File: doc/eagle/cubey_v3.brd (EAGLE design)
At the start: 65 x 56 mm, 24 parts, among them K1 PIN20X2

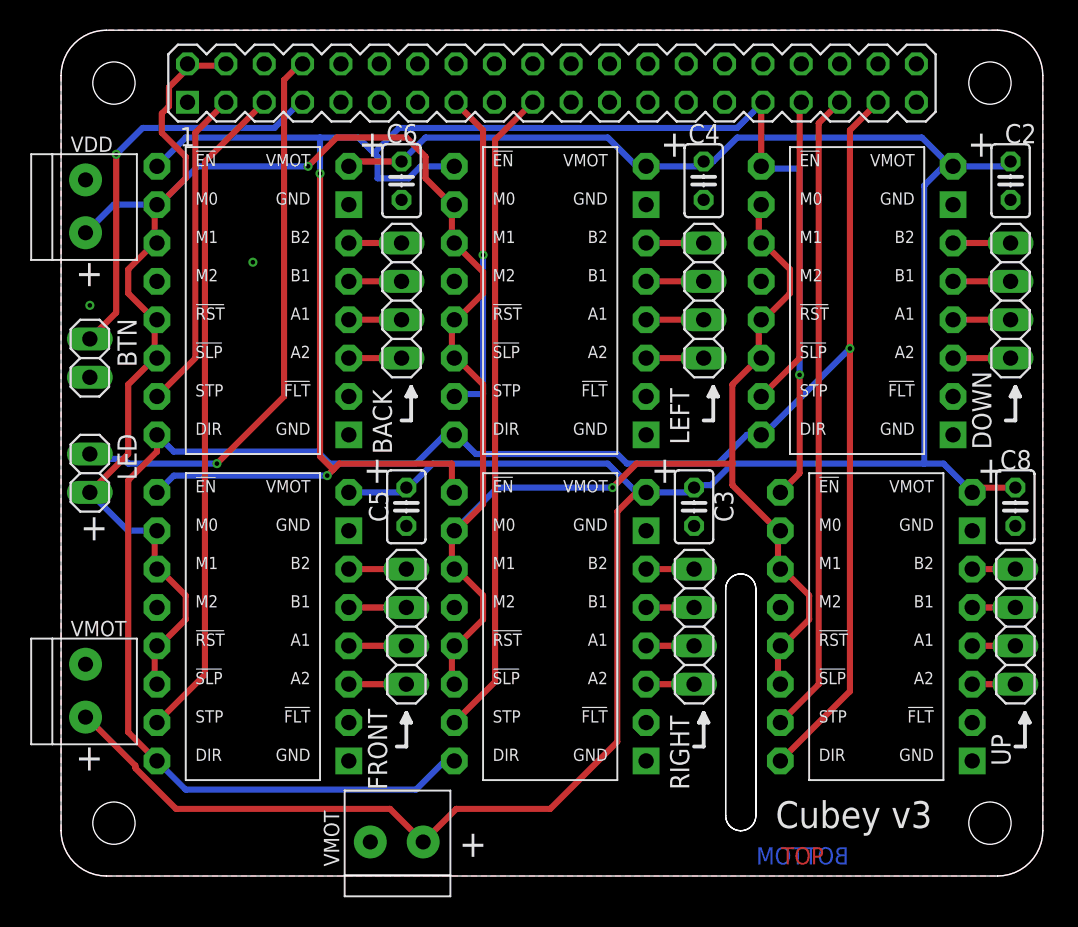
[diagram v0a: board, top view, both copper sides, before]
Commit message: Update v3 board layout, with cutout for RPi camera, remove of v2 designs
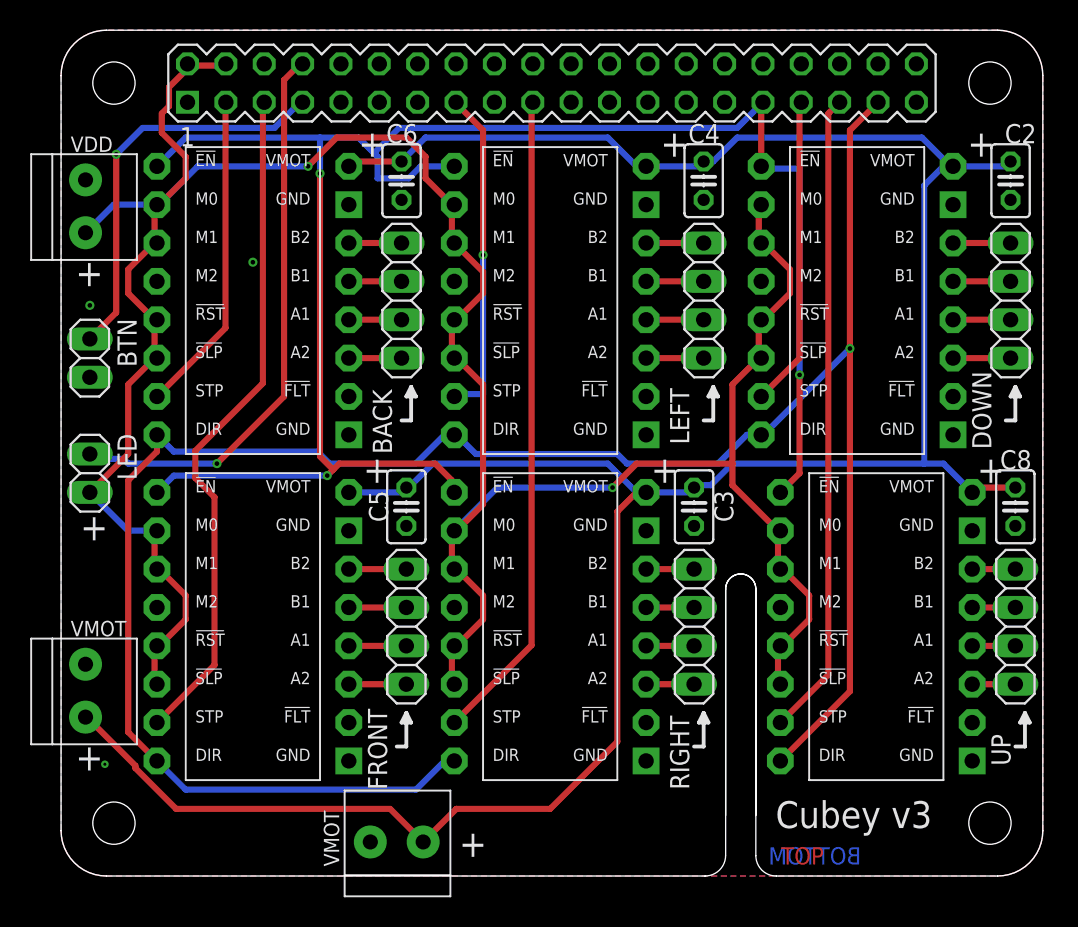
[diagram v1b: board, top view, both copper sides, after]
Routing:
- net FRONT: track 44.0 -> 45.1 mm
- net !EN_MOT: track 123.4 -> 122.7 mm
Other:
- outline, holes or cut-outs redrawn

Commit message: updated board layout
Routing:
- net LEFT: track 22.0 -> 21.0 mm
- net +5V: track 180.6 -> 179.7 mm
- net !EN_MOT: track 122.7 -> 122.2 mm
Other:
- outline, holes or cut-outs redrawn
